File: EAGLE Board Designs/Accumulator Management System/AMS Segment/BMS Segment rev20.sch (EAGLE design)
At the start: 165 parts, among them J1 CONNECTOR-2_MICROFIT_SMD_RIGH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, J10 CONNECTOR-2_MICROFIT_SMD_RIGH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, J100 CONNECTOR-1_5222_, J101 CONNECTOR-1_5222_, J102 CONNECTOR-1_5222_, J103 CONNECTOR-1_5222_, J104 CONNECTOR-1_5222_, J105 CONNECTOR-1_5222_, J106 CONNECTOR-1_5222_, J107 CONNECTOR-1_5222_, J108 CONNECTOR-1_5222_, J109 CONNECTOR-1_5222_, J11 CONNECTOR-2_MICROFIT_SMD_RIGH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, J110 CONNECTOR-1_5222_, J111 CONNECTOR-1_5222_, J112 CONNECTOR-1_5222_, J113 CONNECTOR-1_5222_, J114 CONNECTOR-1_5222_, J115 CONNECTOR-1_5222_, J116 CONNECTOR-1_5222_, J117 CONNECTOR-1_5222_, J118 CONNECTOR-1_5222_, J119 CONNECTOR-1_5222_, J12 CONNECTOR-2_MICROFIT_SMD_RIGH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, J120 CONNECTOR-1_5222_, J121 CONNECTOR-1_5222_, J2 CONNECTOR-2_MICROFIT_SMD_RIGH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, J3 CONNECTOR-2_MICROFIT_SMD_RIGH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, J4 CONNECTOR-2_MICROFIT_SMD_RIGH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, J6 CONNECTOR-2_MICROFIT_SMD_RIGH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, J8 CONNECTOR-2_MICROFIT_SMD_RIGH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, J9 CONNECTOR-2_MICROFIT_SMD_RIGH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, T2 TRANSFORMER_HM2112ZNLT, U1 SHT31-ARP-B, U2 LTC6811-1, U3 LT3990-5, U4 LT3990-5, U5 LTC6811-1, U6 SHT31-ARP-B

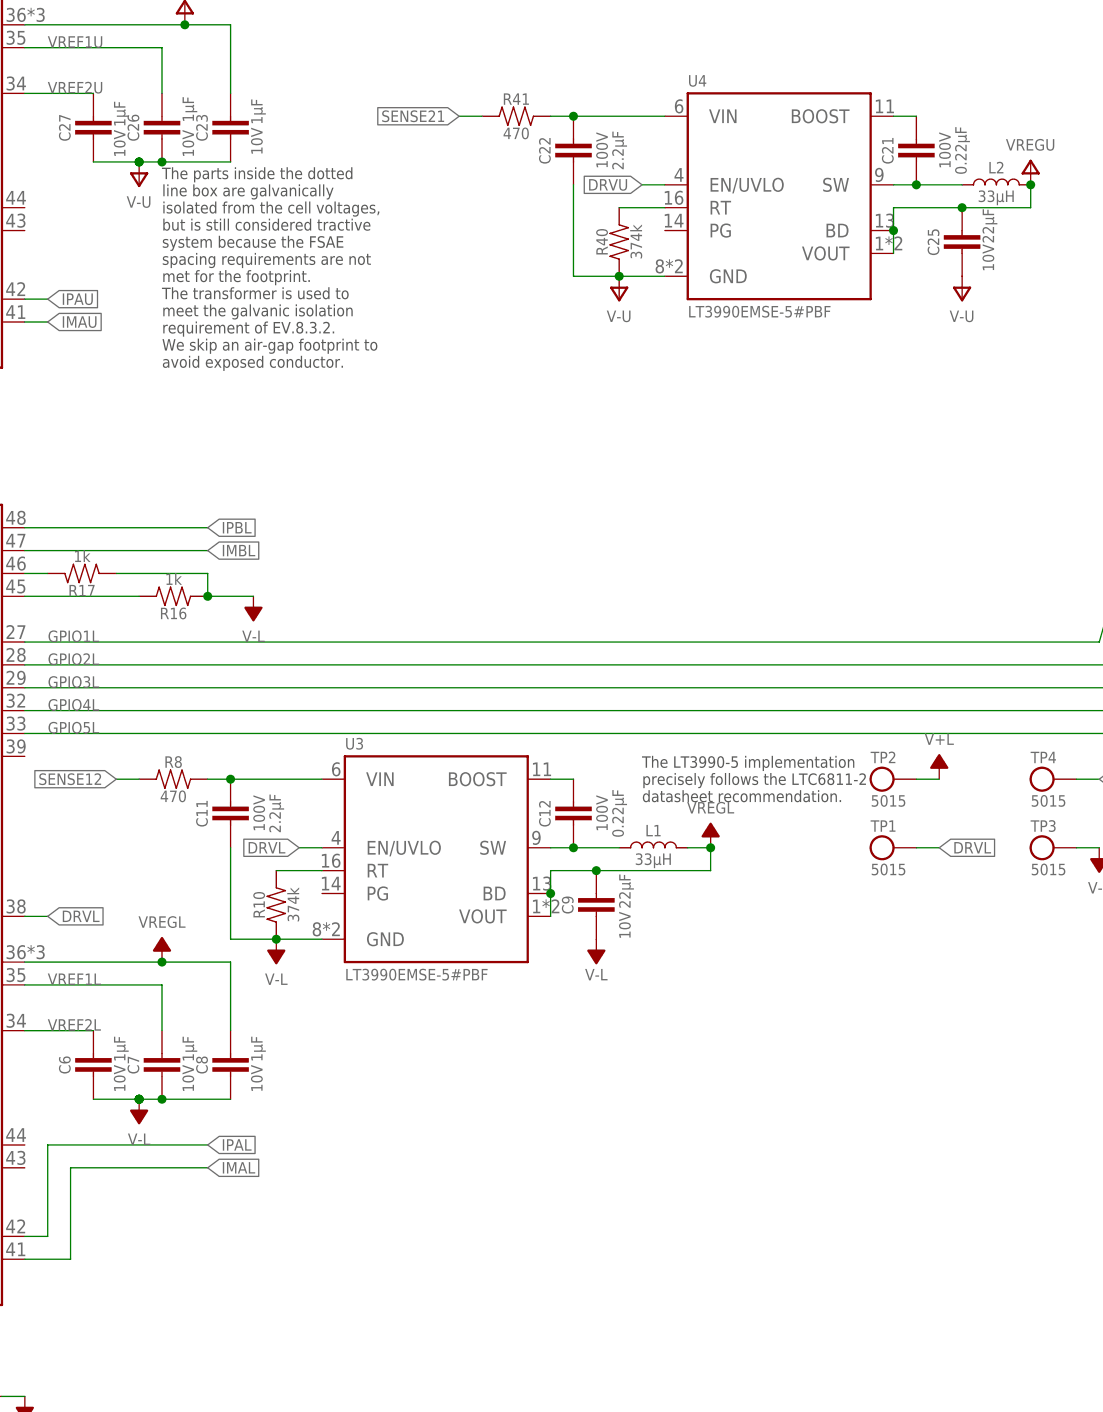
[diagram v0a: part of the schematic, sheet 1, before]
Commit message: Updated Frames
Updated Frame names for changed sheets.
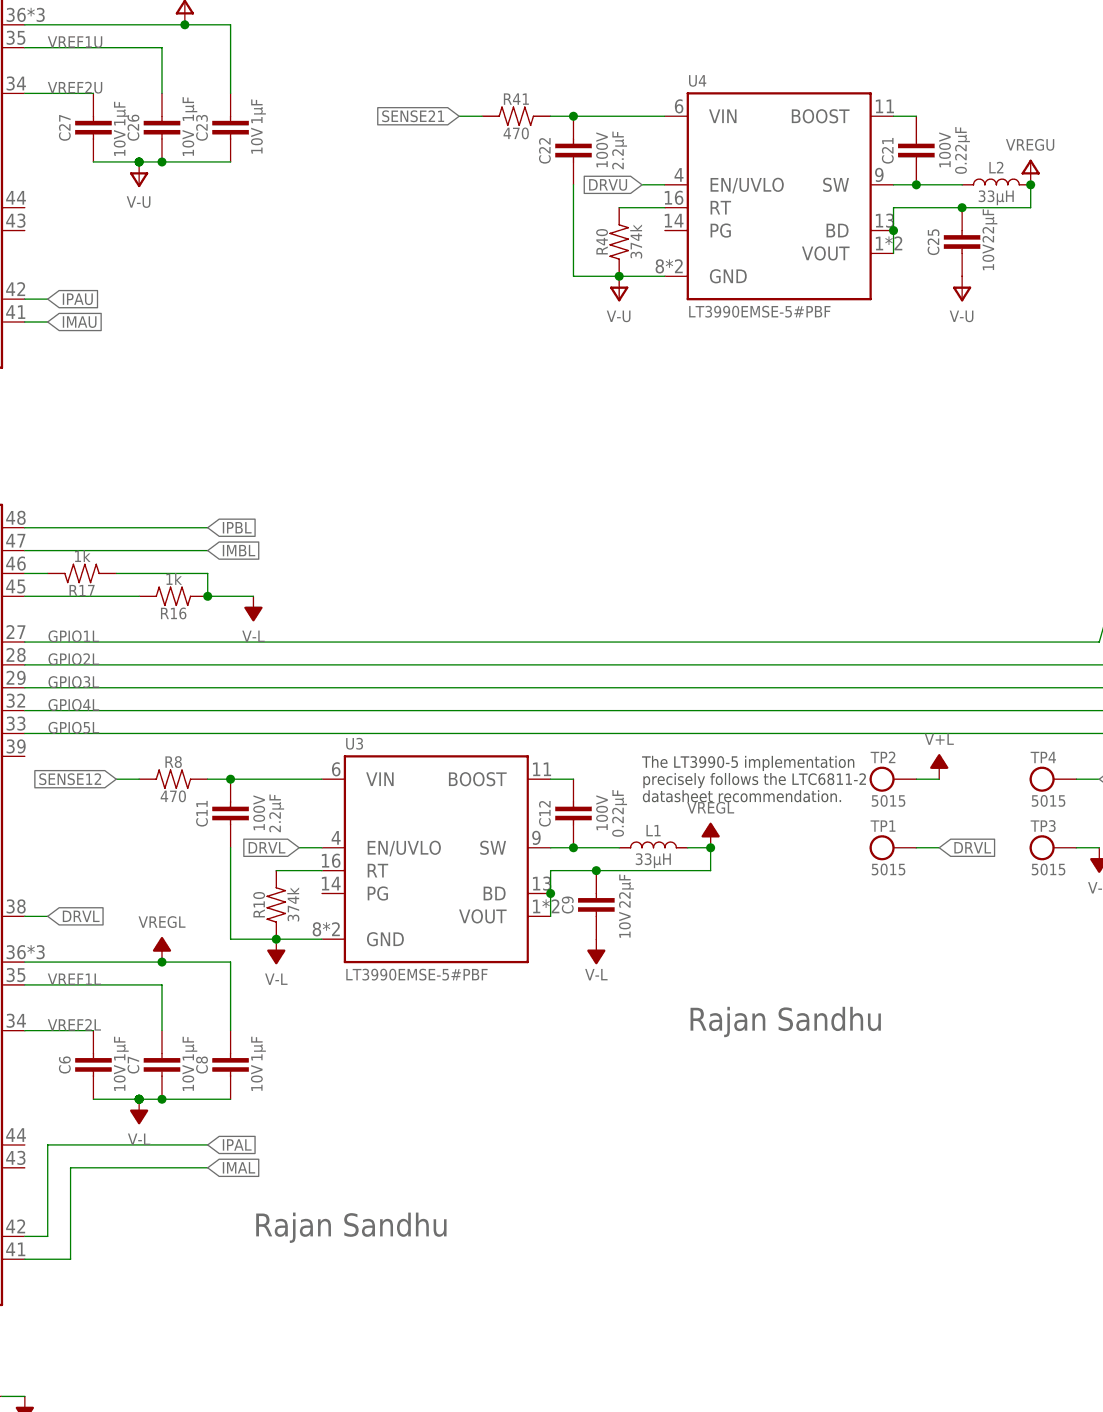
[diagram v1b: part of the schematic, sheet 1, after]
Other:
- note added: "Circuitry for daisy chain connection between boards."
- note added: "Rajan Sandhu"
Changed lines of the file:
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@@
 <part name="P96" library="HyTechSupplies" deviceset="V-U" device=""/>
 <part name="P97" library="HyTechSupplies" deviceset="VREGU" device=""/>
-<part name="U$34" library="HyTechFrames" deviceset="FRAME_SCHEMATIC_ONLY" device="">
-<attribute name="DESCRIPTION_1" value="Ordering Information for off board components"/>
-<attribute name="DESIGNER_SCHEMATIC" value="Cody Kaminsky"/>
-<attribute name="ENGINEER" value="Cody Kaminsky"/>
-<attribute name="REVIEWER_SCHEMATIC" value="Ethan Weinstock"/>
-</part>
 <part name="J11" library="HyTechDevices" deviceset="CONNECTOR-2_?_*" device="MICROFIT_SMD_RIGHTANGLE_02_SINGLE" technology="BLACK" value="CONNECTOR-2_MICROFIT_SMD_RIGHTANGLE_02_SINGLE_BLACK"/>
 <part name="C34" library="HyTechDevices" deviceset="CAPACITOR_?_*" device="0603" technology="10V_10NF"/>
@@
 <part name="TP15" library="HyTechDevices" deviceset="TEST_POINT" device=""/>
 <part name="TP16" library="HyTechDevices" deviceset="TEST_POINT" device=""/>
+<part name="U$34" library="HyTechFrames" deviceset="FRAME_SCHEMATIC_ONLY" device=""/>
 </parts>
 <sheets>
@@
 the lower IC in a situation where a
 fuse blows. The behavior of floating voltage is unknown.</text>
-<text x="119.38" y="119.38" size="1.27" layer="97">The parts inside the dotted
-line box are galvanically
-isolated from the cell voltages,
-but is still considered tractive
-system because the FSAE
-spacing requirements are not
-met for the footprint.
-The transformer is used to
-meet the galvanic isolation
-requirement of EV.8.3.2.
-We skip an air-gap footprint to
-avoid exposed conductor.</text>
 <text x="226.06" y="127" size="1.27" layer="97">The thermistors are done on the
 pull-up side as to not overload
@@
 precisely follows the LTC6811-2
 datasheet recommendation.</text>
+<text x="129.54" y="22.86" size="2.54" layer="95">Rajan Sandhu</text>
+<text x="177.8" y="45.72" size="2.54" layer="95">Rajan Sandhu</text>
 </plain>
 <moduleinsts>
@@
 <attribute name="DRAWING_NAME" x="207.01" y="22.86" size="2.54" layer="95"/>
 <attribute name="SHEET" x="259.08" y="2.54" size="2.54" layer="95"/>
-<attribute name="ENGINEER" x="129.54" y="22.86" size="2.54" layer="95"/>
-<attribute name="DESIGNER_SCHEMATIC" x="176.53" y="45.72" size="2.54" layer="95"/>
-<attribute name="DESIGNER_BOARD" x="176.53" y="38.1" size="2.54" layer="95"/>
 <attribute name="DESIGNER_FURTHER" x="176.53" y="30.48" size="2.54" layer="95"/>
-<attribute name="REVIEWER_SCHEMATIC" x="227.33" y="45.72" size="2.54" layer="95"/>
-<attribute name="REVIEWER_BOARD" x="227.33" y="38.1" size="2.54" layer="95"/>
 <attribute name="REVIEWER_FURTHER" x="227.33" y="30.48" size="2.54" layer="95"/>
 <attribute name="DESCRIPTION_1" x="196.85" y="15.24" size="2.54" layer="95"/>
@@
 We skip an air-gap footprint to
 avoid exposed conductor.</text>
+<text x="177.8" y="30.48" size="2.54" layer="95">Rajan Sandhu</text>
+<text x="195.58" y="10.16" size="2.54" layer="95">Circuitry for daisy chain connection between
+boards.</text>
 </plain>
 <instances>
-<instance part="U$34" gate="G$1" x="0" y="0" smashed="yes">
-<attribute name="LAST_DATE_TIME" x="186.69" y="2.54" size="2.54" layer="95"/>
-<attribute name="DRAWING_NAME" x="207.01" y="22.86" size="2.54" layer="95"/>
-<attribute name="SHEET" x="259.08" y="2.54" size="2.54" layer="95"/>
-<attribute name="ENGINEER" x="129.54" y="22.86" size="2.54" layer="95"/>
-<attribute name="DESIGNER_SCHEMATIC" x="176.53" y="30.48" size="2.54" layer="95"/>
-<attribute name="REVIEWER_SCHEMATIC" x="227.33" y="30.48" size="2.54" layer="95"/>
-<attribute name="DESCRIPTION_1" x="196.85" y="15.24" size="2.54" layer="95"/>
-<attribute name="DESCRIPTION_2" x="176.53" y="10.16" size="2.54" layer="95"/>
-</instance>
 <instance part="J11" gate="G$1" x="139.7" y="157.48" smashed="yes" rot="MR0">
 <attribute name="NAME" x="139.7" y="158.242" size="1.27" layer="95" rot="MR0"/>
@@
 <attribute name="MPN" x="139.7" y="46.482" size="1.27" layer="95" align="top-left"/>
 </instance>
+<instance part="U$34" gate="G$1" x="0" y="0" smashed="yes">
+<attribute name="LAST_DATE_TIME" x="186.69" y="2.54" size="2.54" layer="95"/>
+<attribute name="DRAWING_NAME" x="207.01" y="22.86" size="2.54" layer="95"/>
+<attribute name="SHEET" x="259.08" y="2.54" size="2.54" layer="95"/>
+<attribute name="ENGINEER" x="129.54" y="22.86" size="2.54" layer="95"/>
+<attribute name="DESIGNER_SCHEMATIC" x="176.53" y="30.48" size="2.54" layer="95"/>
+<attribute name="REVIEWER_SCHEMATIC" x="227.33" y="30.48" size="2.54" layer="95"/>
+<attribute name="DESCRIPTION_1" x="196.85" y="15.24" size="2.54" layer="95"/>
+<attribute name="DESCRIPTION_2" x="176.53" y="10.16" size="2.54" layer="95"/>
+</instance>
 </instances>

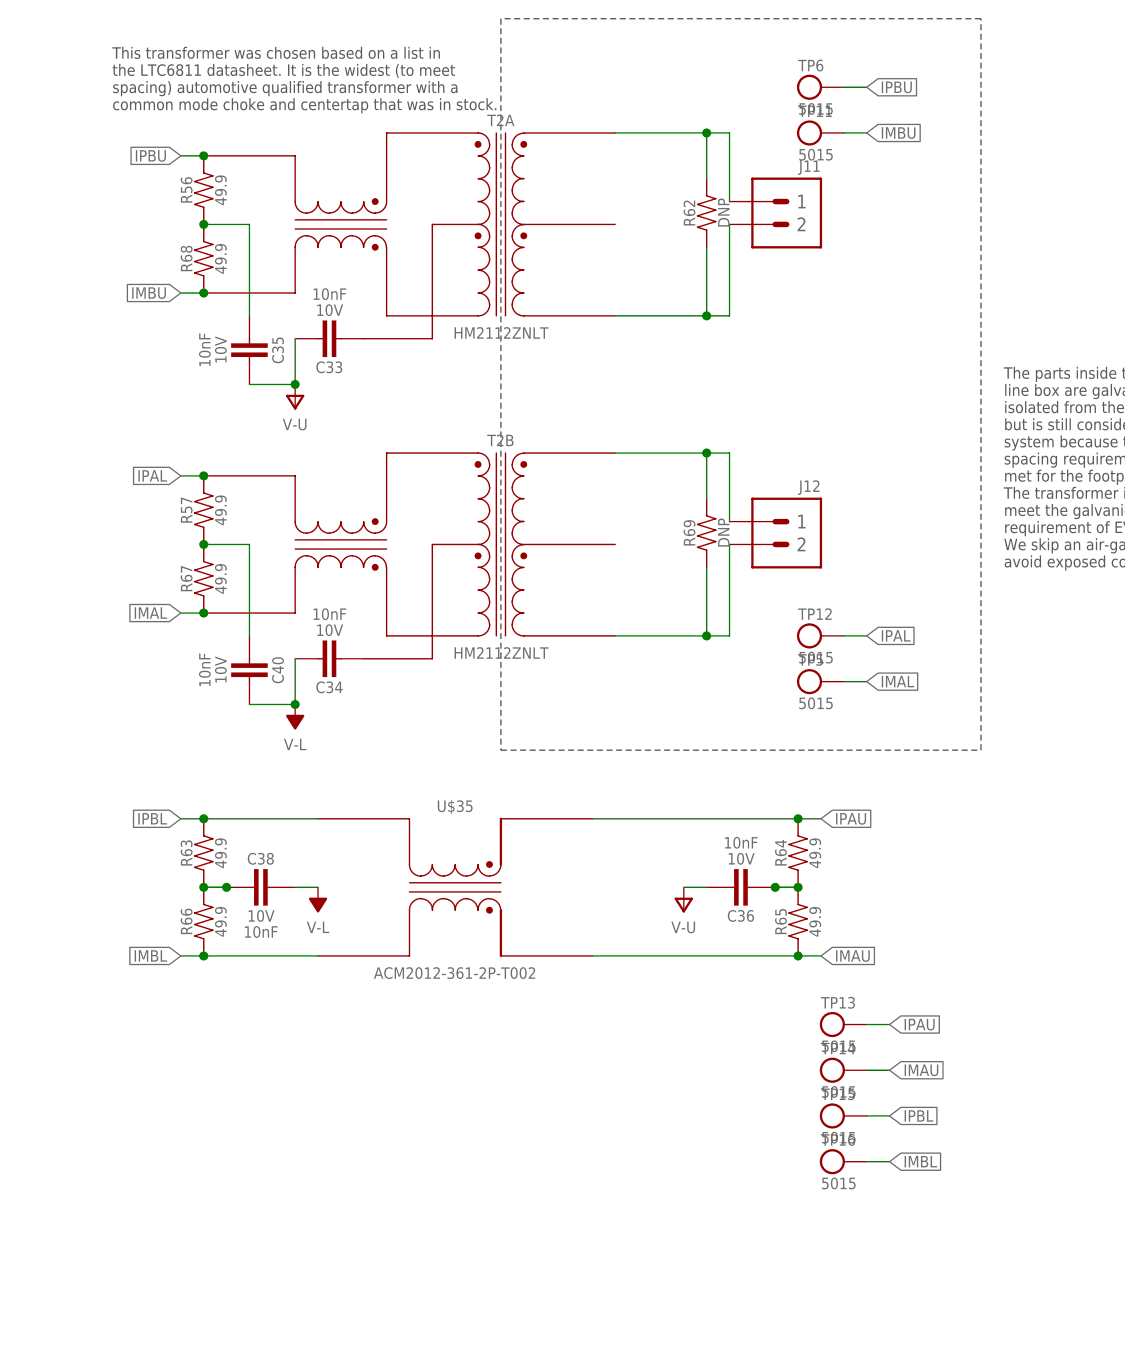
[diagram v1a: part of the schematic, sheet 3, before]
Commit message: Test Point and Termination Update
Got rid of test points -- will use exposed pads on DNP resistors instead -- DNP resistors can be used for termination on last chip as well.
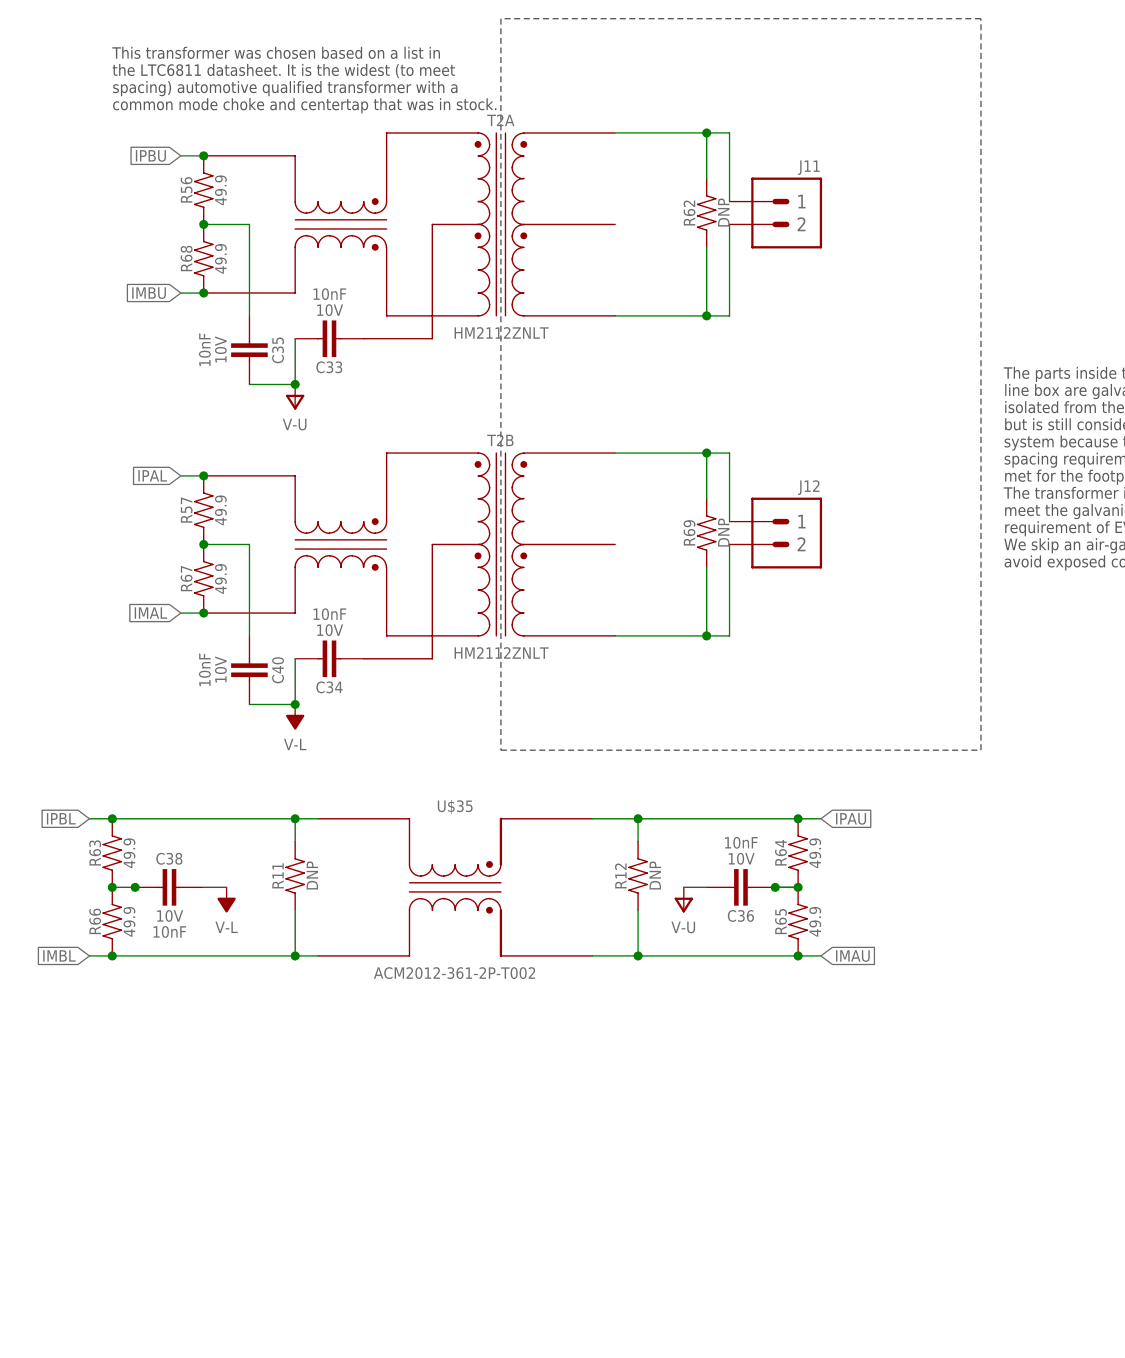
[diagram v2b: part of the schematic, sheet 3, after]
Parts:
- removed TP11, TP12, TP13, TP14, TP15, TP16, TP5, TP6: TEST_POINT, HyTechDevices:TEST_POINT
- added R11, R12: RESISTOR_0603_DNP, HyTechDevices:RESISTOR_0603_DNP
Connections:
- net IMAL: no longer TP5.P$1
- net IMAU: now also R12.1; no longer TP14.P$1
- net IMBL: now also R11.1; no longer TP16.P$1
- net IMBU: no longer TP11.P$1
- net IPAL: no longer TP12.P$1
- net IPAU: now also R12.2; no longer TP13.P$1
- net IPBL: now also R11.2; no longer TP15.P$1
- net IPBU: no longer TP6.P$1
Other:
- moved on the sheet: C38, R63, R66
